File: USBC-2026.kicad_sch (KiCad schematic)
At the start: 0 parts

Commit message: Imported MAX77958 symbol and footprint.
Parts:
- added U1: MAX77958EWV+T, 21-100339_W302B3+1_ADI, symbol symbol_library:MAX77958EWV+T
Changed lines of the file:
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@@
 	(generator_version "10.0")
 	(paper "A4")
+	(symbol
+		(lib_id "symbol_library:MAX77958EWV+T")
+		(at 114.3 83.82 0)
+		(unit 1)
+		(body_style 1)
+		(exclude_from_sim no)
+		(in_bom yes)
+		(on_board yes)
+		(in_pos_files yes)
+		(dnp no)
+		(fields_autoplaced yes)
+		(property "Reference" "U1"
+			(at 137.16 73.66 0)
+			(show_name no)
+			(do_not_autoplace no)
+			(effects
+				(font
+					(size 1.524 1.524)
+				)
+			)
+		)
+		(property "Value" "MAX77958EWV+T"
+			(at 137.16 76.2 0)
+			(show_name no)
+			(do_not_autoplace no)
+			(effects
+				(font
+					(size 1.524 1.524)
+				)
+			)
+		)
+		(property "Footprint" "21-100339_W302B3+1_ADI"
+			(at 114.3 83.82 0)
+			(hide yes)
+			(show_name no)
+			(do_not_autoplace no)
+			(effects
+				(font
+					(size 1.27 1.27)
+					(italic yes)
+				)
+			)
+		)
+		(property "Datasheet" "MAX77958EWV+T"
+			(at 114.3 83.82 0)
+			(hide yes)
+			(show_name no)
+			(do_not_autoplace no)
+			(effects
+				(font
+					(size 1.27 1.27)
+					(italic yes)
+				)
+			)
+		)
+		(property "Description" ""
+			(at 114.3 83.82 0)
+			(hide yes)
+			(show_name no)
+			(do_not_autoplace no)
+			(effects
+				(font
+					(size 1.27 1.27)
+				)
+			)
+		)
+		(pin "E6"
+		)
+		(pin "E4"
+		)
+		(pin "E2"
+		)
+		(pin "E5"
+		)
+		(pin "C5"
+		)
+		(pin "D6"
+		)
+		(pin "D5"
+		)
+		(pin "B4"
+		)
+		(pin "B3"
+		)
+		(pin "C4"
+		)
+		(pin "D4"
+		)
+		(pin "D3"
+		)
+		(pin "A2"
+		)
+		(pin "A1"
+		)
+		(pin "E1"
+		)
+		(pin "E3"
+		)
+		(pin "D1"
+		)
+		(pin "B1"
+		)
+		(pin "A6"
+		)
+		(pin "A5"
+		)
+		(pin "A4"
+		)
+		(pin "A3"
+		)
+		(pin "B2"
+		)
+		(pin "C3"
+		)
+		(pin "C2"
+		)
+		(pin "C1"
+		)
+		(pin "B6"
+		)
+		(pin "B5"
+		)
+		(pin "C6"
+		)
+		(pin "D2"
+		)
+		(instances
+			(project "USBC-2026"
+				(path "/0c056c42-d02c-4bee-adc4-fcbb18375f33"
+					(reference "U1")
+					(unit 1)
+				)
+			)
+		)
+	)
 	(sheet_instances
 		(path "/"

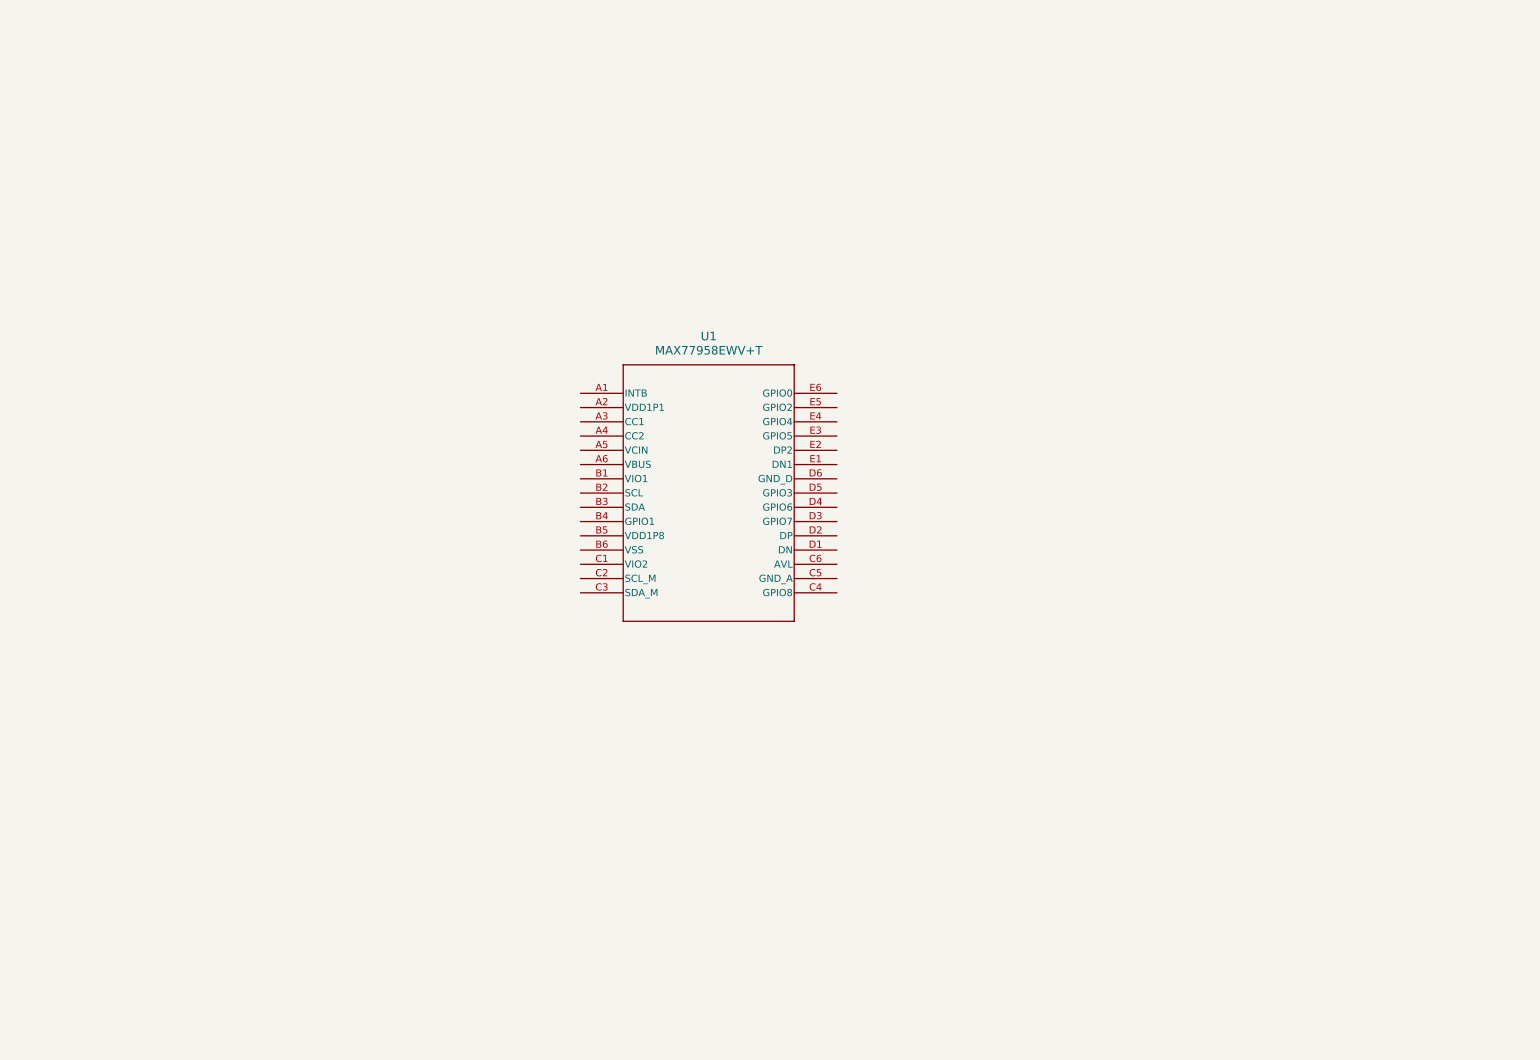
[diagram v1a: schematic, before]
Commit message: Added PDC caps and buck-boost symbol.
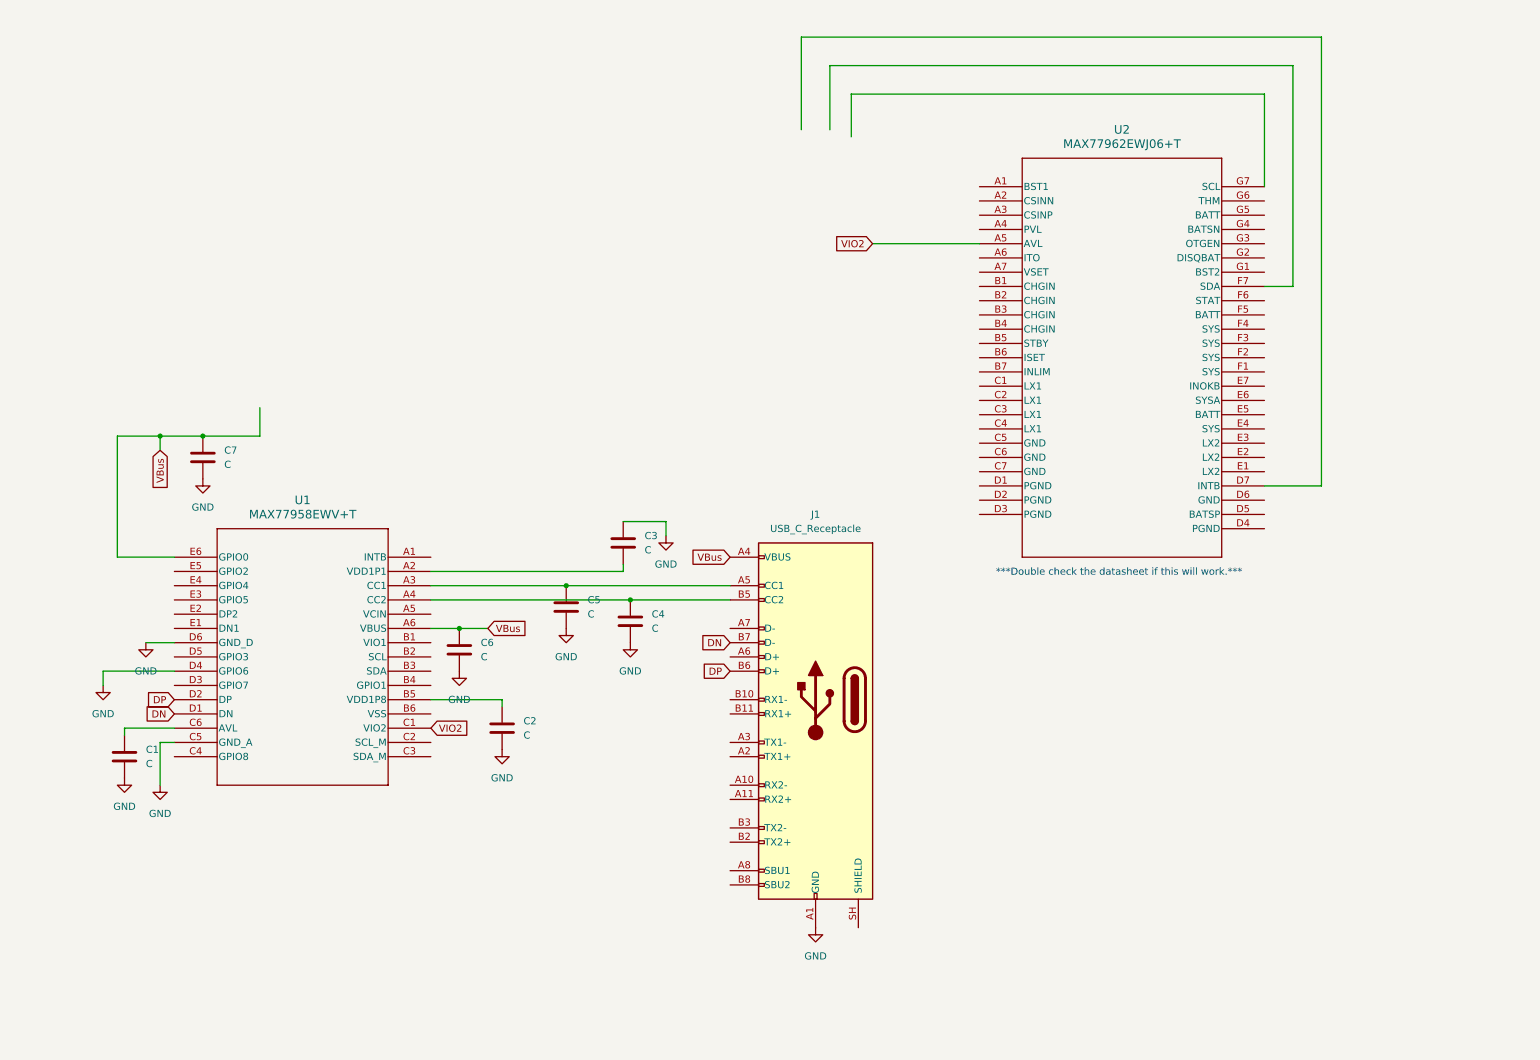
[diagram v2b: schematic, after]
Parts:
- added C1, C2, C3, C4, C5, C6, C7: C, Package_SO:MSOP-8_3x3mm_P0.65mm, symbol Device:C
- added J1: USB_C_Receptacle, symbol Connector:USB_C_Receptacle
- added U2: MAX77962EWJ06+T, 21-100355_MXM, symbol symbol_library:MAX77962EWJ06+T
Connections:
- net at U1.A2 (VDD1P1): now also C3.2
- net at U1.A3 (CC1): now also C5.1, J1.A5 (CC1)
- net at U1.A4 (CC2): now also C4.1, J1.B5 (CC2)
- net VBus: now reaches U1.A6 (VBUS)
- net VBus: now also U1.E6 (GPIO0), C6.1, C7.1, J1.A4 (VBUS), J1.A9 (VBUS), J1.B4 (VBUS), J1.B9 (VBUS)
- net at U1.B5 (VDD1P8): now also C2.1
- net VIO2: now reaches U1.C1 (VIO2)
- net VIO2: now also U2.A5 (AVL)
- net GND: now reaches U1.C5 (GND_A)
- net GND: now also U1.D4 (GPIO6), U1.D6 (GND_D), C1.2, C2.2, C3.1, C4.2, C5.2, C6.2, C7.2, J1.A1 (GND), J1.A12 (GND), J1.B1 (GND), J1.B12 (GND)
- net at U1.C6 (AVL): now also C1.1
- net DN: now reaches U1.D1 (DN)
- net DN: now also J1.B7 (D-)
- net DP: now reaches U1.D2 (DP)
- net DP: now also J1.B6 (D+)
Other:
- note added: "***Double check the datasheet if this will work.***"
- moved on the sheet: U1

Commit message: Updated schematic note about power converter(Needs to be replaced).
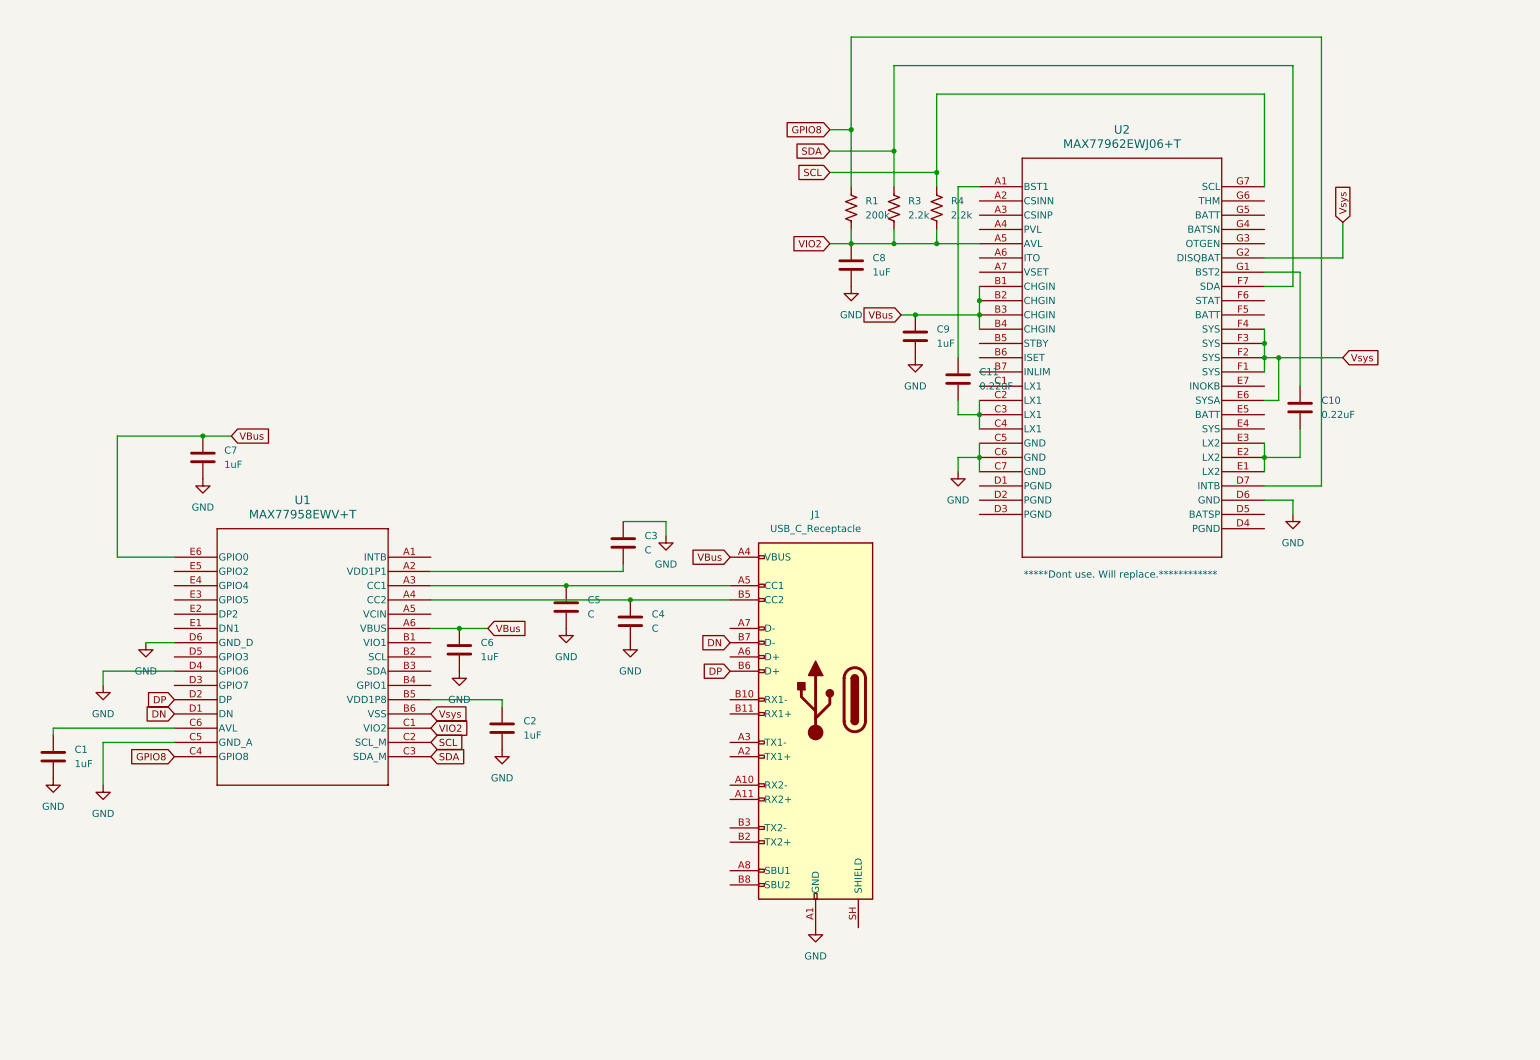
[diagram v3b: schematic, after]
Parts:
- added C10, C11: 0.22uF, Package_SO:MSOP-8_3x3mm_P0.65mm, symbol Device:C
- added C8, C9: 1uF, Package_SO:MSOP-8_3x3mm_P0.65mm, symbol Device:C
- added R1: 200k, Resistor_THT:R_Array_SIP6, symbol Device:R_US
- added R3, R4: 2.2k, Resistor_THT:R_Array_SIP6, symbol Device:R_US
- C1, C2, C6, C7: value C -> 1uF
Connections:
- net GND: now also U2.C5 (GND), U2.C6 (GND), U2.C7 (GND), U2.D6 (GND), C8.2, C9.2
- net VBus: now also U2.B1 (CHGIN), U2.B2 (CHGIN), U2.B3 (CHGIN), U2.B4 (CHGIN), C9.1
- net VIO2: now also C8.1, R1.2, R3.2, R4.2
- net at U2.A1 (BST1): now also C11.1
- net at U2.C2 (LX1): now also U2.C3 (LX1), U2.C4 (LX1), C11.2
- net GPIO8: now reaches U2.D7 (INTB)
- net GPIO8: now also U1.C4 (GPIO8), R1.1
- net at U2.E1 (LX2): now also U2.E2 (LX2), U2.E3 (LX2), C10.2
- net Vsys: now reaches U2.E6 (SYSA)
- net Vsys: now also U1.B6 (VSS), U2.F1 (SYS), U2.F2 (SYS), U2.F3 (SYS), U2.F4 (SYS), U2.G2 (DISQBAT)
- net SDA: now reaches U2.F7 (SDA)
- net SDA: now also U1.C3 (SDA_M), R3.1
- net at U2.G1 (BST2): now also C10.1
- net SCL: now reaches U2.G7 (SCL)
- net SCL: now also U1.C2 (SCL_M), R4.1
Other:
- note added: "*****Dont use. Will replace.************"
- note removed: "***Double check the datasheet if this will work.***"
- moved on the sheet: C1

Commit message: Removed and updated USB pd IC.
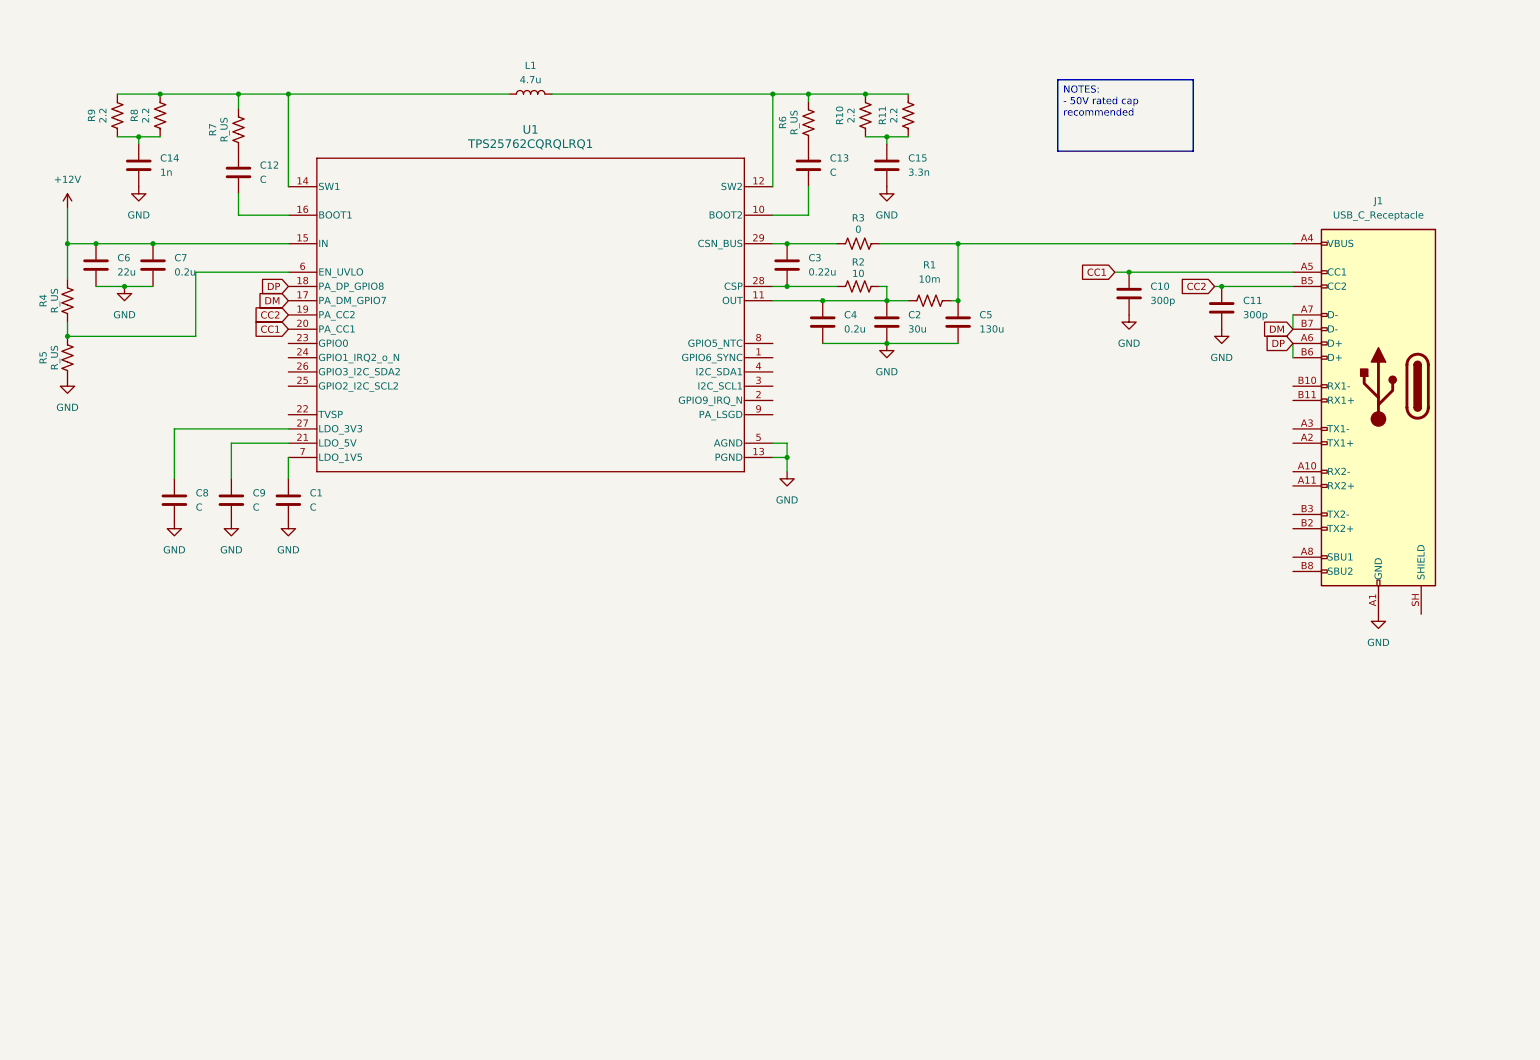
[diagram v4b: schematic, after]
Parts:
- removed U1: MAX77958EWV+T, 21-100339_W302B3+1_ADI, symbol symbol_library:MAX77958EWV+T
- removed U2: MAX77962EWJ06+T, 21-100355_MXM, symbol symbol_library:MAX77962EWJ06+T
- added C12, C13: C, Package_TO_SOT_SMD:SOT-23-5, symbol Device:C
- added C14: 1n, Package_TO_SOT_SMD:SOT-23-5, symbol Device:C
- added C15: 3.3n, Package_TO_SOT_SMD:SOT-23-5, symbol Device:C
- added L1: 4.7u, symbol Device:L
- added R10, R11, R8, R9: 2.2, Resistor_THT:R_Array_SIP4, symbol Device:R_US
- added R2: 10, Resistor_THT:R_Array_SIP4, symbol Device:R_US
- added R5, R6, R7: R_US, Resistor_THT:R_Array_SIP4, symbol Device:R_US
- added U1: TPS25762CQRQLRQ1, RQL0029A-MFG, symbol symbol_library:TPS25762CQRQLRQ1
- C1, C8, C9: value 1uF -> C; footprint Package_SO:MSOP-8_3x3mm_P0.65mm -> Package_TO_SOT_SMD:SOT-23-5
- C10, C11: value 0.22uF -> 300p; footprint Package_SO:MSOP-8_3x3mm_P0.65mm -> Package_TO_SOT_SMD:SOT-23-5
- C2: value 1uF -> 30u; footprint Package_SO:MSOP-8_3x3mm_P0.65mm -> Package_TO_SOT_SMD:SOT-23-5
- C3: value C -> 0.22u; footprint Package_SO:MSOP-8_3x3mm_P0.65mm -> Package_TO_SOT_SMD:SOT-23-5
- C4: value C -> 0.2u; footprint Package_SO:MSOP-8_3x3mm_P0.65mm -> Package_TO_SOT_SMD:SOT-23-5
- C5: value C -> 130u; footprint Package_SO:MSOP-8_3x3mm_P0.65mm -> Package_TO_SOT_SMD:SOT-23-5
- C6: value 1uF -> 22u; footprint Package_SO:MSOP-8_3x3mm_P0.65mm -> Package_TO_SOT_SMD:SOT-23-5
- C7: value 1uF -> 0.2u; footprint Package_SO:MSOP-8_3x3mm_P0.65mm -> Package_TO_SOT_SMD:SOT-23-5
- R1: value 200k -> 10m; footprint Resistor_THT:R_Array_SIP6 -> Resistor_THT:R_Array_SIP4
- R3: value 2.2k -> 0; footprint Resistor_THT:R_Array_SIP6 -> Resistor_THT:R_Array_SIP4
- R4: value 2.2k -> R_US; footprint Resistor_THT:R_Array_SIP6 -> Resistor_THT:R_Array_SIP4
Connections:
- net DN is gone; now on net DM: J1.B7 (D-)
- net GPIO8 is gone; now on an unnamed net: R1.1
- net DP: now also J1.A6 (D+), U1.18 (PA_DP_GPIO8)
- net GND: now also C10.2, C11.2, C14.2, C15.2, R5.1, U1.13 (PGND), U1.5 (AGND); no longer C3.1
- net CC2: now reaches C11.1
- net CC2: now also J1.B5 (CC2), U1.19 (PA_CC2)
- net CC1: now reaches C10.1
- net CC1: now also J1.A5 (CC1), U1.20 (PA_CC1)
- net at C1.1: now also U1.7 (LDO_1V5)
- net at C5.1: now also J1.A4 (VBUS), J1.A9 (VBUS), J1.B4 (VBUS), J1.B9 (VBUS), R1.2, R3.2; no longer J1.A5 (CC1)
- net DM: now reaches J1.A7 (D-)
- net DM: now also U1.17 (PA_DM_GPIO7)
- net at C4.1: now also C2.1, R2.2, U1.11 (OUT); no longer J1.B5 (CC2)
- net at C3.2: now also R2.1, U1.28 (CSP)
- net SCL: no longer names the net of R4.1
- net SCL: now also R5.2, U1.6 (EN_UVLO)
- net SDA: no longer names the net of R3.1
- net SDA: now also C3.1, U1.29 (CSN_BUS)
- removed net VBus: C6.1, C7.1, C9.1, J1.A4 (VBUS), J1.A9 (VBUS), J1.B4 (VBUS), J1.B9 (VBUS)
- removed net VIO2: C8.1, R1.2, R3.2, R4.2
- new net: C15.1, R10.1, R11.1
- new net: L1.2, R10.2, R11.2, R6.2, U1.12 (SW2)
- new net: C12.1, R7.1
- new net: C12.2, U1.16 (BOOT1)
- new net: L1.1, R7.2, R8.2, R9.2, U1.14 (SW1)
- new net: C13.1, R6.1
- new net: C8.1, U1.27 (LDO_3V3)
- new net: C9.1, U1.21 (LDO_5V)
- new net: C13.2, U1.10 (BOOT2)
- new net: C14.1, R8.1, R9.1
- new net +12V: C6.1, C7.1, R4.2, U1.15 (IN)
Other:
- note removed: "*****Dont use. Will replace.************"
- moved on the sheet: J1
